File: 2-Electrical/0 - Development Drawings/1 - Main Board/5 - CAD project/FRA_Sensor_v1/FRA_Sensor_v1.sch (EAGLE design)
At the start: 213 parts, among them IC1 CP2101, IC2 ADS1115IDGSR, IC3 P82B715DR, IC4 ADS1115IDGSR, IC5 ADS1115IDGSR, IC8 PCA9555PW, IC9 LDK320ADU50R, J2 ETH_CONN, J3 PJ-059A, J4 DNI, J5 WM9734TR-ND, J8 1140084168, J9 4pin, Q10 FDN306P, Q11 FDN306P, Q12 FDN306P, Q13 FDN306P, Q14 FDN306P, Q15 FDN306P, Q2 FDN306P, Q3 Si2300DS, Q5 FDN306P, Q6 FDN306P, Q7 DNI, Q8 FDN306P, Q9 FDN306P, T1 BC847, T2 BC847, U1 PCA9509DP, U2 ESP-WROOM-32, X1 TB001-500-02BE, Y3 DNI

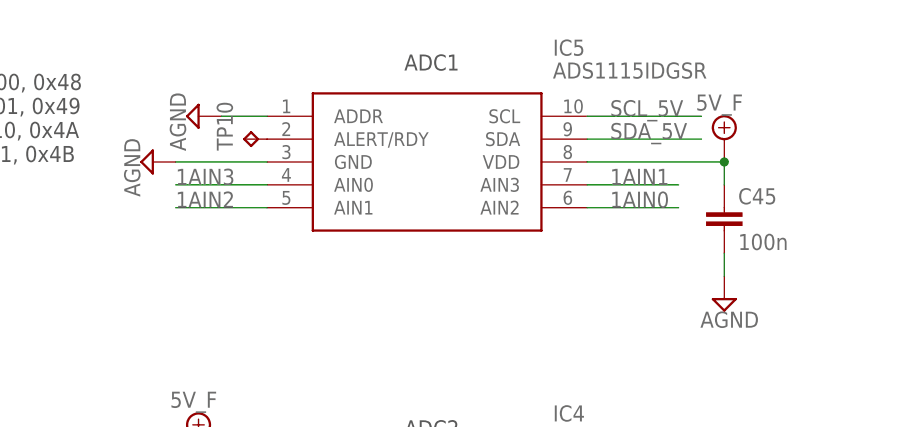
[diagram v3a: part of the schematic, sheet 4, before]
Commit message: updates
amonia sensor
preparation for LMP91000
ADC1 address changed to match V4 board
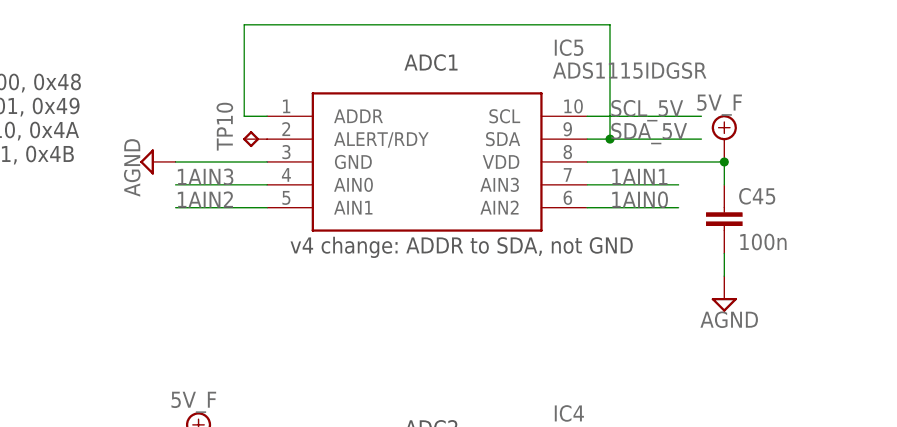
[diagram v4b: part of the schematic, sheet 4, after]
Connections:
- net AGND: no longer IC5.ADDR
- net SDA_5V: now also IC5.ADDR
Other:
- note added: "v4 change: ADDR to SDA, not GND"
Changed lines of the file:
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@@
 <attributes>
 <attribute name="CNAME" value="FRA Sensor Unit"/>
-<attribute name="CREVISION" value="03"/>
+<attribute name="CREVISION" value="04"/>
 </attributes>
 <variantdefs>
@@
 </part>
 <part name="SUPPLY143" library="supply2" deviceset="AGND" device=""/>
-<part name="SUPPLY144" library="supply2" deviceset="AGND" device=""/>
 <part name="SUPPLY145" library="supply2" deviceset="+5V/1" device="" value="5V_F"/>
 <part name="SUPPLY146" library="supply2" deviceset="AGND" device=""/>
@@
 <text x="116.84" y="104.14" size="1.778" layer="97">ADC3</text>
 <text x="114.3" y="63.5" size="1.778" layer="97">A3.0,A3.3</text>
+<text x="104.14" y="154.94" size="1.778" layer="97">v4 change: ADDR to SDA, not GND</text>
 </plain>
 <instances>
@@
 </instance>
 <instance part="SUPPLY143" gate="G$1" x="88.9" y="165.1" rot="R270"/>
-<instance part="SUPPLY144" gate="G$1" x="93.98" y="170.18" rot="R270"/>
 <instance part="SUPPLY145" gate="G$1" x="93.98" y="134.62"/>
 <instance part="SUPPLY146" gate="G$1" x="55.88" y="12.7"/>
@@
 <segment>
 <pinref part="IC5" gate="G$1" pin="SDA"/>
-<wire x1="137.16" y1="167.64" x2="149.86" y2="167.64" width="0.1524" layer="91"/>
+<wire x1="137.16" y1="167.64" x2="139.7" y2="167.64" width="0.1524" layer="91"/>
 <label x="139.7" y="167.64" size="1.778" layer="95"/>
+<pinref part="IC5" gate="G$1" pin="ADDR"/>
+<wire x1="139.7" y1="167.64" x2="149.86" y2="167.64" width="0.1524" layer="91"/>
+<wire x1="101.6" y1="170.18" x2="99.06" y2="170.18" width="0.1524" layer="91"/>
+<wire x1="99.06" y1="170.18" x2="99.06" y2="180.34" width="0.1524" layer="91"/>
+<wire x1="99.06" y1="180.34" x2="139.7" y2="180.34" width="0.1524" layer="91"/>
+<wire x1="139.7" y1="180.34" x2="139.7" y2="167.64" width="0.1524" layer="91"/>
+<junction x="139.7" y="167.64"/>
 </segment>
 <segment>
@@
 </segment>
 <segment>
-<pinref part="SUPPLY144" gate="G$1" pin="AGND"/>
-<pinref part="IC5" gate="G$1" pin="ADDR"/>
-<wire x1="96.52" y1="170.18" x2="101.6" y2="170.18" width="0.1524" layer="91"/>
-</segment>
-<segment>

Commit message: hw design updates
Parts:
- C19: value 100n -> DNI
- D1, D2, D4, D6: value PESD1CAN -> PESD1CANSC70; device diode:PESD1CAN -> diode:PESD1CANSC70
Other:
- note added: "unfiltered for Amonia sensor"
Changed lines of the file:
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@@
 <grid distance="0.1" unitdist="inch" unit="inch" style="lines" multiple="1" display="no" altdistance="0.01" altunitdist="inch" altunit="inch"/>
 <layers>
-<layer number="1" name="Top" color="4" fill="1" visible="no" active="no"/>
-<layer number="2" name="Route2" color="1" fill="3" visible="no" active="no"/>
-<layer number="3" name="Route3" color="4" fill="3" visible="no" active="no"/>
-<layer number="4" name="Route4" color="1" fill="4" visible="no" active="no"/>
-<layer number="5" name="Route5" color="4" fill="4" visible="no" active="no"/>
-<layer number="6" name="Route6" color="1" fill="8" visible="no" active="no"/>
-<layer number="7" name="Route7" color="4" fill="8" visible="no" active="no"/>
-<layer number="8" name="Route8" color="1" fill="2" visible="no" active="no"/>
-<layer number="9" name="Route9" color="4" fill="2" visible="no" active="no"/>
-<layer number="10" name="Route10" color="1" fill="7" visible="no" active="no"/>
-<layer number="11" name="Route11" color="4" fill="7" visible="no" active="no"/>
-<layer number="12" name="Route12" color="1" fill="5" visible="no" active="no"/>
-<layer number="13" name="Route13" color="4" fill="5" visible="no" active="no"/>
-<layer number="14" name="Route14" color="1" fill="6" visible="no" active="no"/>
-<layer number="15" name="Route15" color="4" fill="6" visible="no" active="no"/>
-<layer number="16" name="Bottom" color="1" fill="1" visible="no" active="no"/>
-<layer number="17" name="Pads" color="2" fill="1" visible="no" active="no"/>
-<layer number="18" name="Vias" color="2" fill="1" visible="no" active="no"/>
-<layer number="19" name="Unrouted" color="6" fill="1" visible="no" active="no"/>
-<layer number="20" name="Dimension" color="15" fill="1" visible="no" active="no"/>
-<layer number="21" name="tPlace" color="7" fill="1" visible="no" active="no"/>
-<layer number="22" name="bPlace" color="7" fill="1" visible="no" active="no"/>
-<layer number="23" name="tOrigins" color="15" fill="1" visible="no" active="no"/>
-<layer number="24" name="bOrigins" color="15" fill="1" visible="no" active="no"/>
-<layer number="25" name="tNames" color="58" fill="1" visible="no" active="no"/>
-<layer number="26" name="bNames" color="7" fill="1" visible="no" active="no"/>
-<layer number="27" name="tValues" color="7" fill="1" visible="no" active="no"/>
-<layer number="28" name="bValues" color="7" fill="1" visible="no" active="no"/>
+<layer number="1" name="Top" color="4" fill="1" visible="yes" active="no"/>
+<layer number="2" name="Route2" color="1" fill="3" visible="yes" active="no"/>
+<layer number="3" name="Route3" color="4" fill="3" visible="yes" active="no"/>
+<layer number="4" name="Route4" color="1" fill="4" visible="yes" active="no"/>
+<layer number="5" name="Route5" color="4" fill="4" visible="yes" active="no"/>
+<layer number="6" name="Route6" color="1" fill="8" visible="yes" active="no"/>
+<layer number="7" name="Route7" color="4" fill="8" visible="yes" active="no"/>
+<layer number="8" name="Route8" color="1" fill="2" visible="yes" active="no"/>
+<layer number="9" name="Route9" color="4" fill="2" visible="yes" active="no"/>
+<layer number="10" name="Route10" color="1" fill="7" visible="yes" active="no"/>
+<layer number="11" name="Route11" color="4" fill="7" visible="yes" active="no"/>
+<layer number="12" name="Route12" color="1" fill="5" visible="yes" active="no"/>
+<layer number="13" name="Route13" color="4" fill="5" visible="yes" active="no"/>
+<layer number="14" name="Route14" color="1" fill="6" visible="yes" active="no"/>
+<layer number="15" name="Route15" color="4" fill="6" visible="yes" active="no"/>
+<layer number="16" name="Bottom" color="1" fill="1" visible="yes" active="no"/>
+<layer number="17" name="Pads" color="2" fill="1" visible="yes" active="no"/>
+<layer number="18" name="Vias" color="2" fill="1" visible="yes" active="no"/>
+<layer number="19" name="Unrouted" color="6" fill="1" visible="yes" active="no"/>
+<layer number="20" name="Dimension" color="15" fill="1" visible="yes" active="no"/>
+<layer number="21" name="tPlace" color="7" fill="1" visible="yes" active="no"/>
+<layer number="22" name="bPlace" color="7" fill="1" visible="yes" active="no"/>
+<layer number="23" name="tOrigins" color="15" fill="1" visible="yes" active="no"/>
+<layer number="24" name="bOrigins" color="15" fill="1" visible="yes" active="no"/>
+<layer number="25" name="tNames" color="58" fill="1" visible="yes" active="no"/>
+<layer number="26" name="bNames" color="7" fill="1" visible="yes" active="no"/>
+<layer number="27" name="tValues" color="7" fill="1" visible="yes" active="no"/>
+<layer number="28" name="bValues" color="7" fill="1" visible="yes" active="no"/>
 <layer number="29" name="tStop" color="7" fill="3" visible="no" active="no"/>
 <layer number="30" name="bStop" color="7" fill="6" visible="no" active="no"/>
@@
 <layer number="35" name="tGlue" color="7" fill="4" visible="no" active="no"/>
 <layer number="36" name="bGlue" color="7" fill="5" visible="no" active="no"/>
-<layer number="37" name="tTest" color="7" fill="1" visible="no" active="no"/>
-<layer number="38" name="bTest" color="7" fill="1" visible="no" active="no"/>
+<layer number="37" name="tTest" color="7" fill="1" visible="yes" active="no"/>
+<layer number="38" name="bTest" color="7" fill="1" visible="yes" active="no"/>
 <layer number="39" name="tKeepout" color="4" fill="11" visible="no" active="no"/>
 <layer number="40" name="bKeepout" color="1" fill="11" visible="no" active="no"/>
@@
 <layer number="44" name="Drills" color="7" fill="1" visible="no" active="no"/>
 <layer number="45" name="Holes" color="7" fill="1" visible="no" active="no"/>
-<layer number="46" name="Milling" color="3" fill="1" visible="no" active="no"/>
-<layer number="47" name="Measures" color="7" fill="1" visible="no" active="no"/>
-<layer number="48" name="Document" color="7" fill="1" visible="no" active="no"/>
-<layer number="49" name="Reference" color="7" fill="1" visible="no" active="no"/>
-<layer number="50" name="dxf" color="7" fill="1" visible="no" active="no"/>
-<layer number="51" name="tDocu" color="7" fill="1" visible="no" active="no"/>
-<layer number="52" name="bDocu" color="7" fill="1" visible="no" active="no"/>
-<layer number="53" name="tGND_GNDA" color="7" fill="9" visible="no" active="no"/>
-<layer number="54" name="bGND_GNDA" color="1" fill="9" visible="no" active="no"/>
-<layer number="56" name="wert" color="7" fill="1" visible="no" active="no"/>
-<layer number="57" name="tCAD" color="7" fill="1" visible="no" active="no"/>
-<layer number="59" name="tCarbon" color="7" fill="1" visible="no" active="no"/>
-<layer number="60" name="bCarbon" color="7" fill="1" visible="no" active="no"/>
+<layer number="46" name="Milling" color="3" fill="1" visible="yes" active="no"/>
+<layer number="47" name="Measures" color="7" fill="1" visible="yes" active="no"/>
+<layer number="48" name="Document" color="7" fill="1" visible="yes" active="no"/>
+<layer number="49" name="Reference" color="7" fill="1" visible="yes" active="no"/>
+<layer number="50" name="dxf" color="7" fill="1" visible="yes" active="no"/>
+<layer number="51" name="tDocu" color="7" fill="1" visible="yes" active="no"/>
+<layer number="52" name="bDocu" color="7" fill="1" visible="yes" active="no"/>
+<layer number="53" name="tGND_GNDA" color="7" fill="9" visible="yes" active="no"/>
+<layer number="54" name="bGND_GNDA" color="1" fill="9" visible="yes" active="no"/>
+<layer number="56" name="wert" color="7" fill="1" visible="yes" active="no"/>
+<layer number="57" name="tCAD" color="7" fill="1" visible="yes" active="no"/>
+<layer number="59" name="tCarbon" color="7" fill="1" visible="yes" active="no"/>
+<layer number="60" name="bCarbon" color="7" fill="1" visible="yes" active="no"/>
 <layer number="88" name="SimResults" color="9" fill="1" visible="yes" active="yes"/>
 <layer number="89" name="SimProbes" color="9" fill="1" visible="yes" active="yes"/>
@@
 <attributes>
 <attribute name="CNAME" value="FRA Sensor Unit"/>
-<attribute name="CREVISION" value="04"/>
+<attribute name="CREVISION" value="05"/>
 </attributes>
 <variantdefs>
@@
 <part name="SUPPLY7" library="SparkFun-PowerSymbols" deviceset="3.3V" device=""/>
 <part name="SUPPLY9" library="SparkFun-PowerSymbols" deviceset="V_USB" device=""/>
-<part name="D1" library="diode" deviceset="PESD1CAN" device="">
+<part name="D1" library="diode" deviceset="PESD1CAN" device="SC70" value="PESD1CANSC70">
 <attribute name="PARTNO" value="PESD1CAN-UX"/>
 </part>
-<part name="D2" library="diode" deviceset="PESD1CAN" device="">
+<part name="D2" library="diode" deviceset="PESD1CAN" device="SC70" value="PESD1CANSC70">
 <attribute name="PARTNO" value="PESD1CAN-UX"/>
 </part>
@@
 <part name="TP3" library="testpad" deviceset="TP" device="TP10R"/>
 <part name="TP4" library="testpad" deviceset="TP" device="TP10R"/>
-<part name="D4" library="diode" deviceset="PESD1CAN" device="">
+<part name="D4" library="diode" deviceset="PESD1CAN" device="SC70" value="PESD1CANSC70">
 <attribute name="PARTNO" value="PESD1CAN-UX"/>
 </part>
-<part name="D6" library="diode" deviceset="PESD1CAN" device="">
+<part name="D6" library="diode" deviceset="PESD1CAN" device="SC70" value="PESD1CANSC70">
 <attribute name="PARTNO" value="PESD1CAN-UX"/>
 </part>
@@
 <attribute name="PARTNO" value="CRCW060310K0JNEAC"/>
 </part>
-<part name="C19" library="resistor" deviceset="C-EU" device="C0603K" value="100n">
+<part name="C19" library="resistor" deviceset="C-EU" device="C0603K" value="DNI">
 <attribute name="PARTNO" value="CC0603KRX7R8BB104"/>
 </part>
@@
 <text x="114.3" y="63.5" size="1.778" layer="97">A3.0,A3.3</text>
 <text x="104.14" y="154.94" size="1.778" layer="97">v4 change: ADDR to SDA, not GND</text>
+<text x="259.08" y="76.2" size="1.778" layer="97" font="fixed">unfiltered
+for Amonia
+sensor</text>
 </plain>
 <instances>

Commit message: Update FRA_Sensor_v1.sch
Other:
- note added: "alternative: 75k || 3M"
